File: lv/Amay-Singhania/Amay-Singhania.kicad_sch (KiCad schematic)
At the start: 4 parts

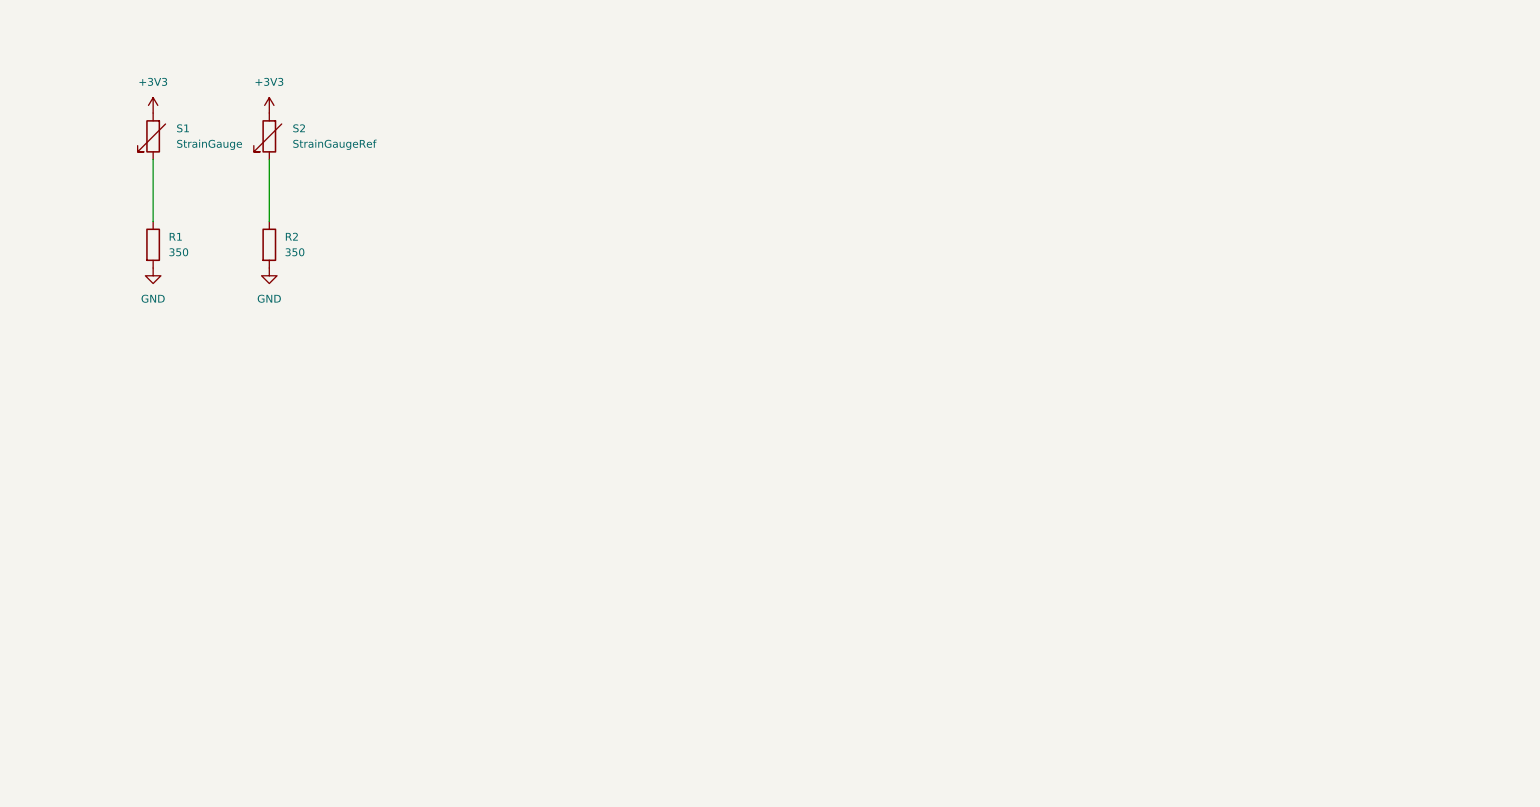
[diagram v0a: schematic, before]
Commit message: large edits to strain gauge LV onboarding project. gauges made; INAs sourced; 6 channel SPI ADC sourced
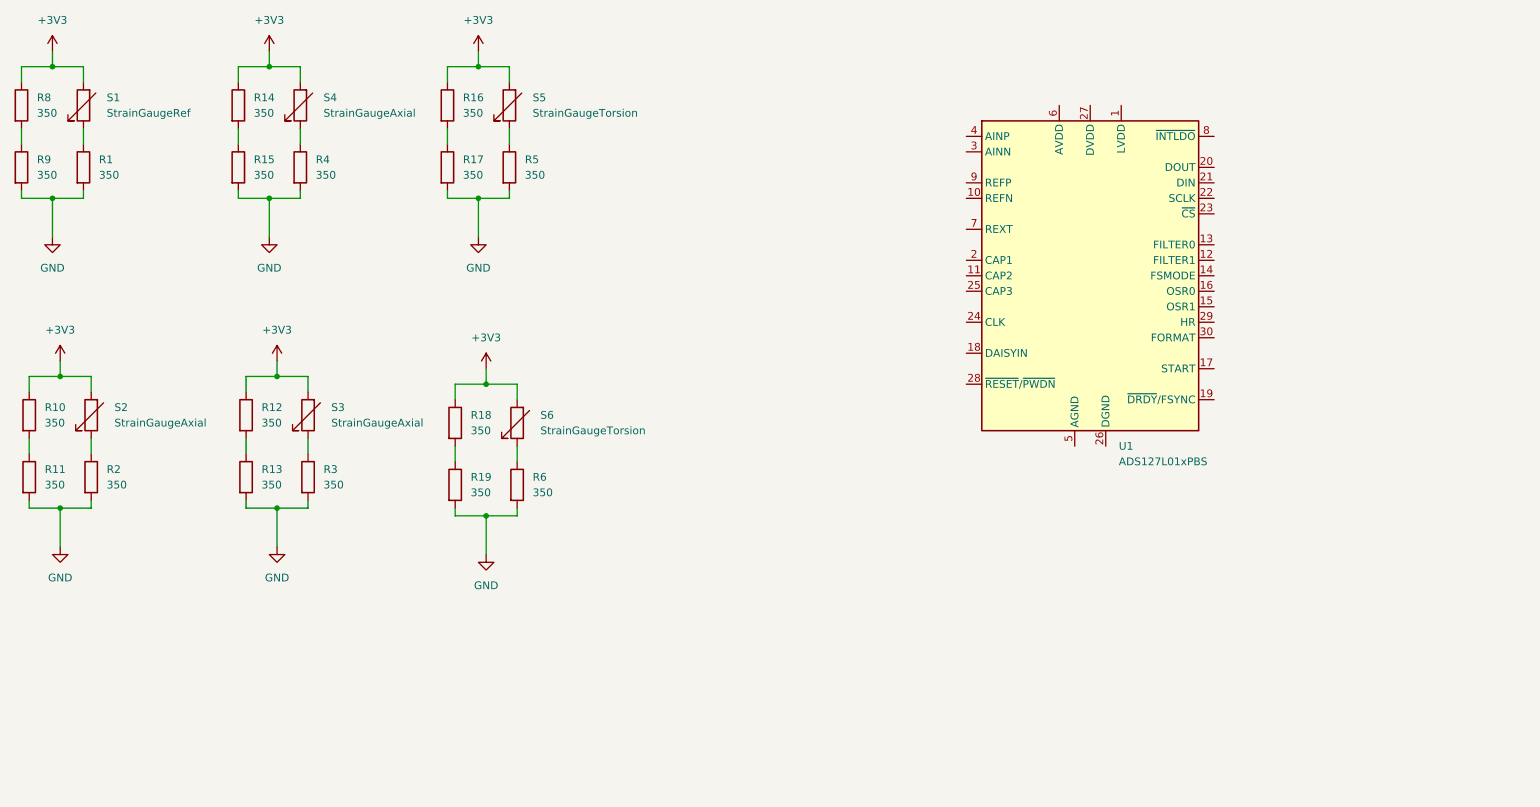
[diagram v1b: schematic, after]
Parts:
- added R10, R11, R12, R13, R14, R15, R16, R17, R18, R19, R3, R4, R5, R6, R8, R9: 350, Resistor_SMD:R_01005_0402Metric, symbol Device:R
- added S3, S4: StrainGaugeAxial, StrainGauge:Strain Gauge V1, symbol Device:R_Variable
- added S5: StrainGaugeTorsion, StrainGauge:TorsionalGauge-45deg, symbol Device:R_Variable
- added S6: StrainGaugeTorsion, StrainGauge:TorsionalGauge45deg, symbol Device:R_Variable
- added U1: ADS127L01xPBS, ADS127L01xPBS:VQFN56_RSH_TEX, symbol Analog_ADC:ADS127L01xPBS
- S1: value StrainGauge -> StrainGaugeRef; footprint StrainGauge:Strain Gauge V1 -> StrainGauge:ReferenceStrainGauge
- S2: value StrainGaugeRef -> StrainGaugeAxial
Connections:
- net +3V3: now also R10.1, R12.1, R14.1, R16.1, R18.1, R8.1, S3.2, S4.2, S5.2, S6.2
- net GND: now also R11.2, R13.2, R15.2, R17.2, R19.2, R3.2, R4.2, R5.2, R6.2, R9.2
- new net: R5.1, S5.1
- new net: R16.2, R17.1
- new net: R4.1, S4.1
- new net: R6.1, S6.1
- new net: R8.2, R9.1
- new net: R12.2, R13.1
- new net: R3.1, S3.1
- new net: R14.2, R15.1
- new net: R18.2, R19.1
- new net: U1.31 (AGND), U1.5 (AGND)
- new net: U1.32 (AVDD), U1.6 (AVDD)
- new net: R10.2, R11.1
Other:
- moved on the sheet: R1, S1, S2

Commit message: wired instrumentation amps and calculated gain measurements
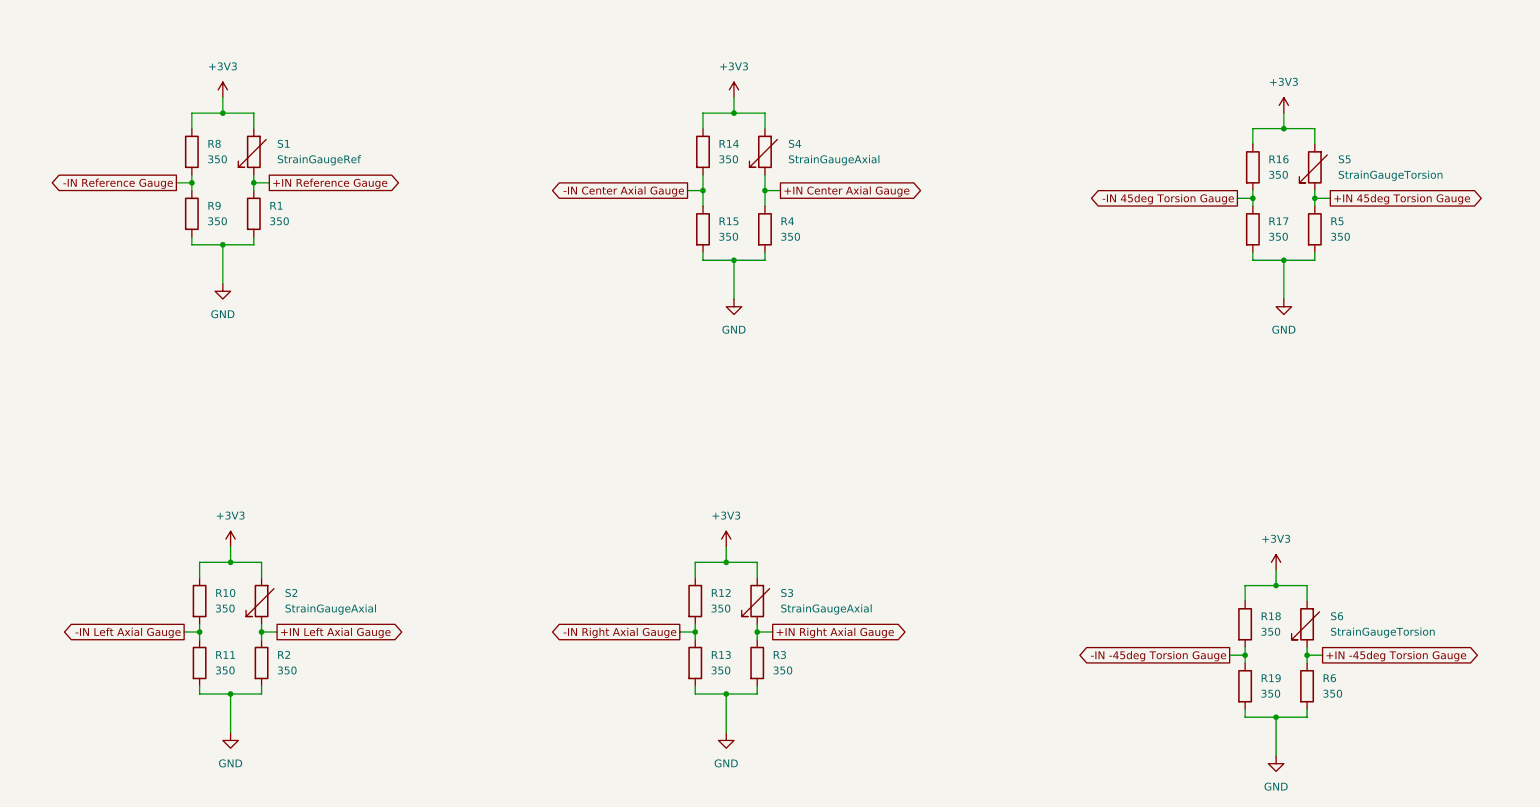
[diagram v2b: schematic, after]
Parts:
- removed U1: ADS127L01xPBS, ADS127L01xPBS:VQFN56_RSH_TEX, symbol Analog_ADC:ADS127L01xPBS
- S5: footprint StrainGauge:TorsionalGauge-45deg -> StrainGauge:TorsionalGauge45deg
- S6: footprint StrainGauge:TorsionalGauge45deg -> StrainGauge:TorsionalGauge-45deg
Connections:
- net +IN 45deg Torsion Gauge: now reaches R5.1, S5.1
- net -IN 45deg Torsion Gauge: now reaches R16.2, R17.1
- net +IN Center Axial Gauge: now reaches R4.1, S4.1
- net +IN -45deg Torsion Gauge: now reaches R6.1, S6.1
- net +IN Reference Gauge: now reaches R1.1, S1.1
- net -IN Reference Gauge: now reaches R8.2, R9.1
- net +IN Left Axial Gauge: now reaches R2.1, S2.1
- net -IN Right Axial Gauge: now reaches R12.2, R13.1
- net +IN Right Axial Gauge: now reaches R3.1, S3.1
- net -IN Center Axial Gauge: now reaches R14.2, R15.1
- net -IN -45deg Torsion Gauge: now reaches R18.2, R19.1
- net -IN Left Axial Gauge: now reaches R10.2, R11.1
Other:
- moved on the sheet: R1, R10, R11, R12, R13, R14, R15, R16, R17, R18, R19, R2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
